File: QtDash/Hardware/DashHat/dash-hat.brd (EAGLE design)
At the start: 120.9 x 74.9 mm, 160 parts, among them IC1 LMV614, IC10 MAX9924, IC11 ZXTR2105FQ, IC2 MCP3X083008, IC3 MCP23017SS, IC4 LM358D, IC5 IL300, IC6 TSV912D, IC7 IL300, IC8 TSV912D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

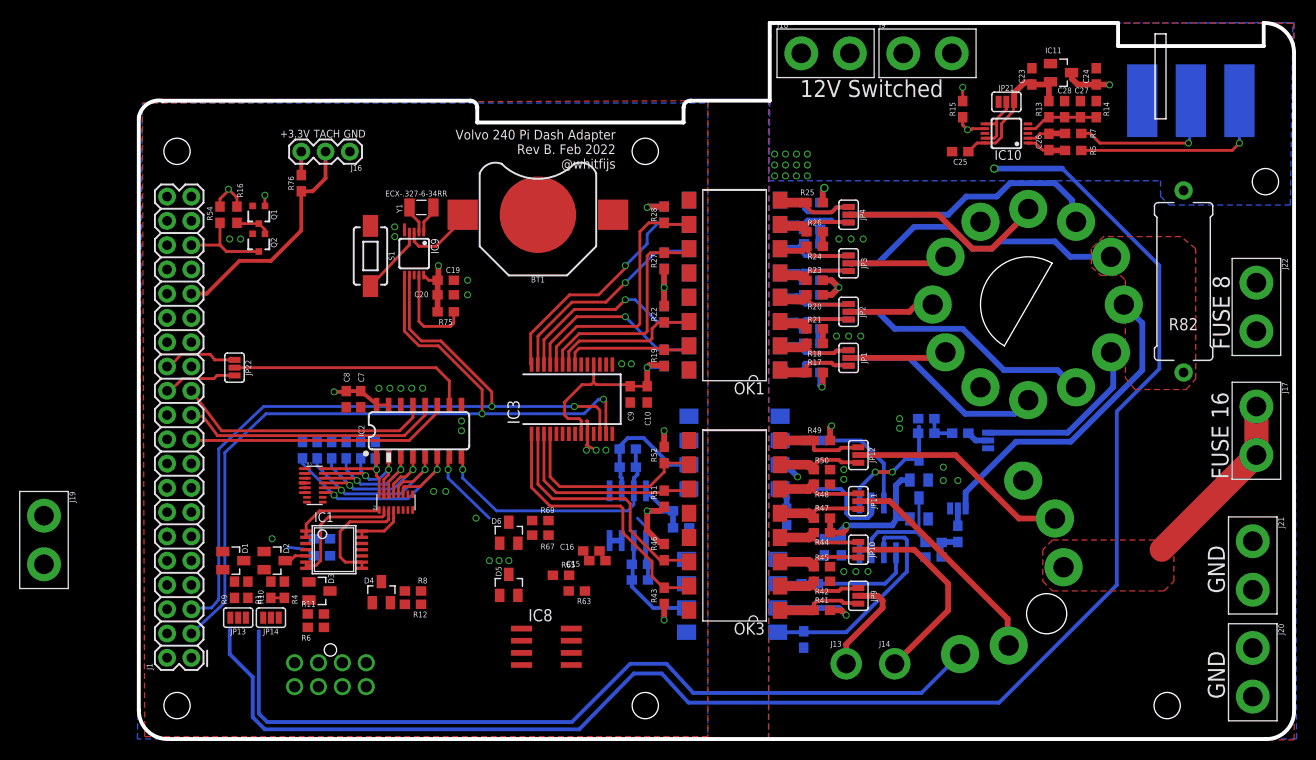
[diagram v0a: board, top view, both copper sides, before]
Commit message: topic/hardware-revc: 	- Analog input layout with new connector is done -- need to check on connector footprint as there is a dimension error 	- TODO: replace switched 12V power and GND with molex connector (right angle?)
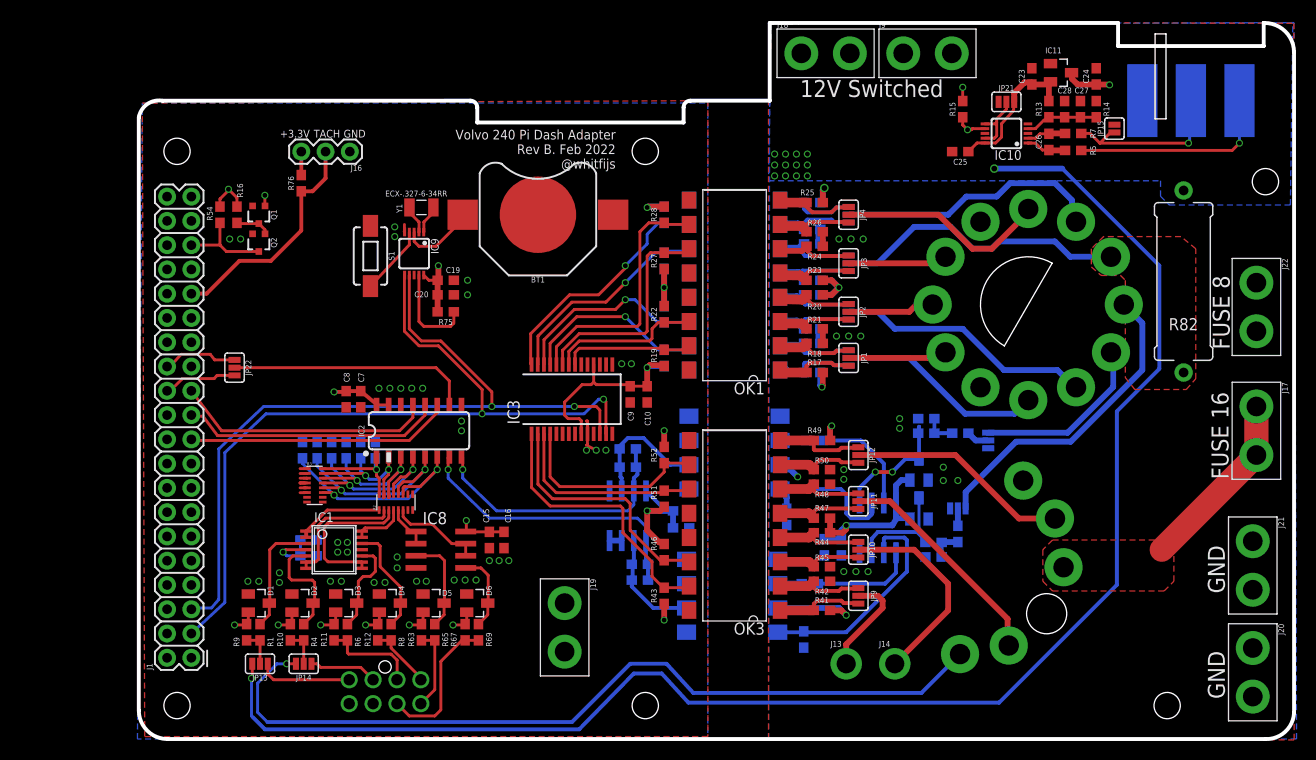
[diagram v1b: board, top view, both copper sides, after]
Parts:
- added JP15: VSS- Jumper, SparkFun-Jumpers:SMT-JUMPER_2_NO_SILK
- moved J19 55.2 mm to (44.7, 11.7)
- moved R63 16.8 mm to (29.7, 11.2), turned to 90 degrees
- moved IC8 15.0 mm to (31.8, 19.8)
- moved R65 14.5 mm to (31.1, 11.2), turned to 90 degrees
- moved R69 13.4 mm to (35.7, 11.2), turned to 90 degrees
- moved R67 12.9 mm to (34.3, 11.2), turned to 90 degrees
- moved C15 11.5 mm to (36.8, 20.8), turned to 270 degrees
- moved C16 9.22 mm to (38.4, 20.8), turned to 270 degrees
- moved D5 8.10 mm to (31.0, 14.2), turned to 270 degrees
- moved D6 8.07 mm to (35.6, 14.2), turned to 270 degrees
- moved J2 5.99 mm to (25.9, 4.95)
- moved JP14 5.92 mm to (17.4, 7.87)
- moved JP13 5.34 mm to (12.8, 7.87)
- moved D2 5.32 mm to (17.3, 14.2)
- moved D1 5.18 mm to (12.7, 14.2)
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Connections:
- net N$48 renamed VSS+
- removed net N$49: J11.1, R7.1
- new net VSS-: J11.1, JP15.1, R7.1
- net 5V: now also J2.7; no longer J2.1
- net GND-ISO: now also JP15.2
- net SENSOR4_IN: now also J2.1; no longer J2.5
- net SENSOR5_IN: now also J2.5; no longer J2.6
- net SENSOR6_IN: now also J2.6; no longer J2.7
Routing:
- net 5V: track 3.27 -> 27.2 mm, vias 0 -> 8
- net VSS-: track 0.00 -> 18.2 mm, vias 0 -> 1
- net N$49: track 16.3 -> 0.00 mm, vias 1 -> 0
- net SIG_3V3_IN1: track 15.4 -> 30.9 mm
- net SENSOR6_IN: track 0.00 -> 15.3 mm
- net N$3: track 0.00 -> 12.3 mm
- net N$15: track 0.00 -> 11.5 mm
- net SENSOR3_IN: track 0.00 -> 10.3 mm
- net N$29: track 0.00 -> 10.3 mm
- net N$11: track 0.00 -> 10.1 mm
- net SENSOR1_IN: track 0.00 -> 9.84 mm
- net N$35: track 0.00 -> 9.69 mm
- net N$7: track 2.42 -> 11.5 mm
- net SENSOR5_IN: track 0.00 -> 8.62 mm
- net N$36: track 0.17 -> 8.21 mm
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
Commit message: topic/hardware-revc: 	- added right angle nano-fit molex connector for switched 12V power 	- added 4 user inputs on the remaining 4 pins of MCP23017 	- added pwm output on pin 18 with 3.3V pullup 	- added user inputs to dash_lights.h -- likely need to pull this out and/or rework
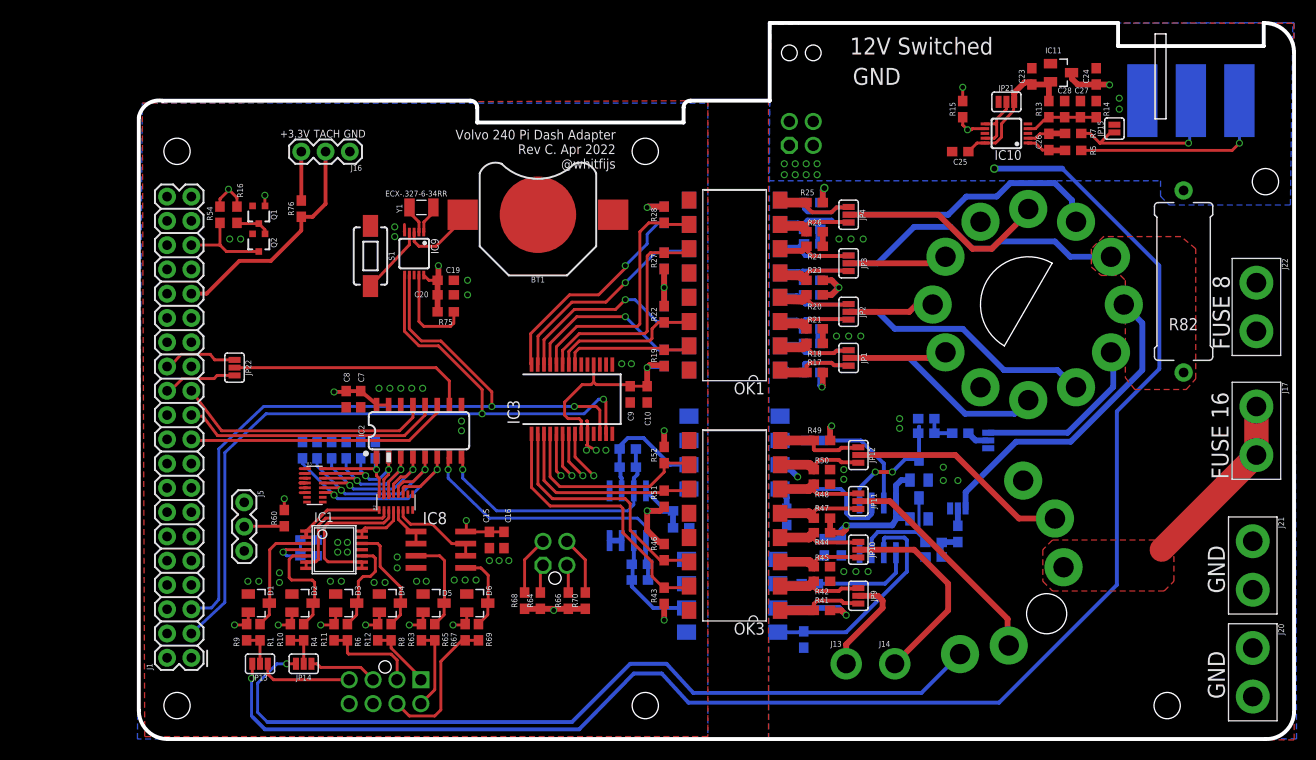
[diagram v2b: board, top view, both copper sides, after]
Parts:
- removed J18, J19, J9: (no value), SparkFun-Connectors:1X02_XTRA_BIG
- added J3: CONN_04RIGHT-ANGLE, digital_dash:MOLEX-1053141204
- added J4: CONN_04, digital_dash:MOLEX-1053101104
- added J5: PWM_OUT, SparkFun-Connectors:1X03
- added R60: 20k, digital_dash:0603
- added R64, R66, R68, R70: 1k, digital_dash:0603
- moved R76 2.67 mm to (17.1, 55.5)
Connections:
- new net GPIO18: J1.12, J5.2, R60.1
- new net USER_IN1: IC3.5, J4.1, R64.2
- new net USER_IN2: IC3.6, J4.2, R66.2
- new net USER_IN3: IC3.7, J4.3, R68.2
- new net USER_IN4: IC3.8, J4.4, R70.2
- net 12V: now also J3.1, J3.2; no longer J18.1, J18.2, J9.1, J9.2
- net 3.3V: now also R60.2, R64.1, R66.1, R68.1, R70.1
- net 5V: now also J5.3; no longer J19.2
- net GND: now also J5.1; no longer J19.1
- net GND-ISO: now also J3.3, J3.4
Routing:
- net USER_IN2: track 0.00 -> 21.6 mm, vias 0 -> 1
- net USER_IN3: track 0.00 -> 19.7 mm, vias 0 -> 1
- net USER_IN1: track 0.00 -> 19.6 mm, vias 0 -> 1
- net USER_IN4: track 0.00 -> 19.5 mm, vias 0 -> 1
- net GPIO18: track 0.00 -> 12.9 mm
- net 3.3V: track 70.9 -> 81.3 mm, vias 9 -> 11
- net AC_RELAY/VSS_TO_ECU: track 111.5 -> 113.5 mm
- net GND-ISO: vias 16 -> 18
- net 12V: vias 21 -> 17
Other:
- board text added: "Volvo 240 Pi Dash Adapter Rev C. Apr 2022 @whitfijs"
- board text removed: "Volvo 240 Pi Dash Adapter Rev B. Feb 2022 @whitfijs"

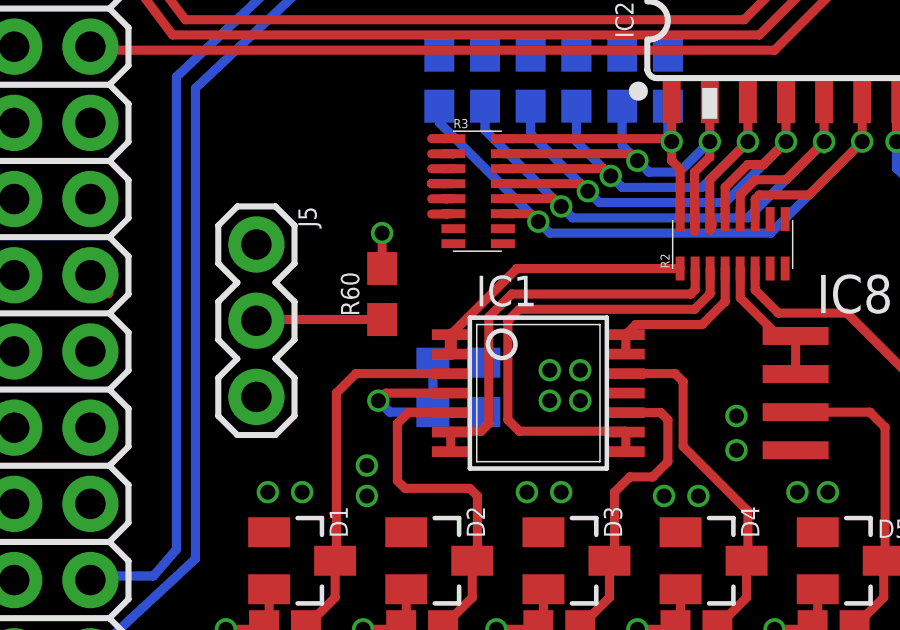
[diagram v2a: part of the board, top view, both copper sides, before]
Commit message: topic/hardware-revc: 	- small layout changes to the main board
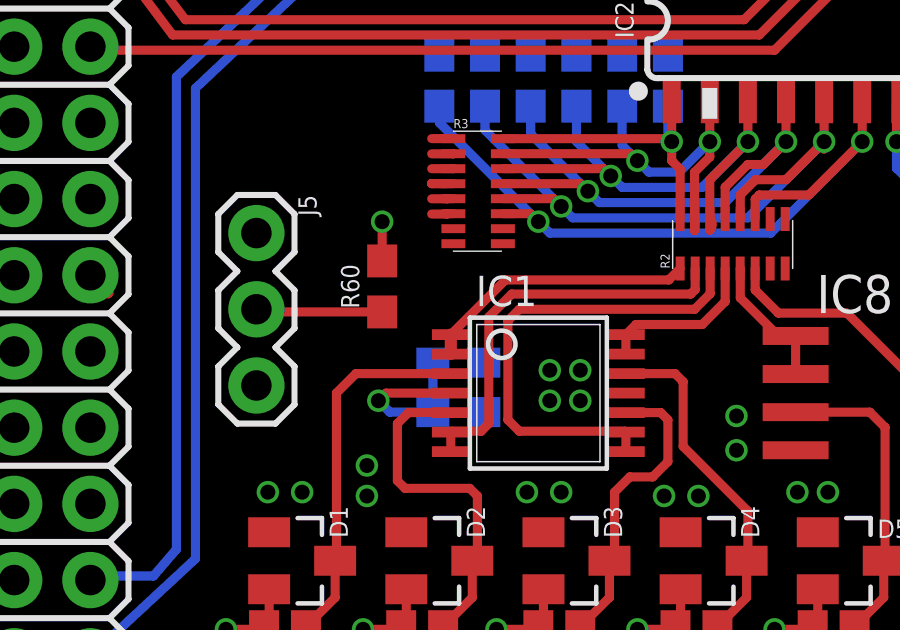
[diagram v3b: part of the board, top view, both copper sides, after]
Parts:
- moved J5 0.38 mm to (11.2, 25.1)
- moved R60 0.25 mm to (15.4, 23.4)
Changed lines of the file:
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@@
 <element name="J3" library="digital_dash" package="MOLEX-1053141204" value="CONN_04RIGHT-ANGLE" x="69.469" y="63.373"/>
 <element name="J4" library="digital_dash" package="MOLEX-1053101104" value="CONN_04" x="43.688" y="19.431" rot="R180"/>
-<element name="J5" library="SparkFun-Connectors" package="1X03" value="PWM_OUT" x="11.176" y="24.765" rot="R270">
-<attribute name="PROD_ID" value="XXX-00000" x="11.176" y="24.765" size="1.778" layer="27" rot="R270" display="off"/>
+<element name="J5" library="SparkFun-Connectors" package="1X03" value="PWM_OUT" x="11.176" y="25.146" rot="R270">
+<attribute name="PROD_ID" value="XXX-00000" x="11.176" y="25.146" size="1.778" layer="27" rot="R270" display="off"/>
 </element>
-<element name="R60" library="digital_dash" package="0603" value="20k" x="15.367" y="23.114" rot="R90"/>
+<element name="R60" library="digital_dash" package="0603" value="20k" x="15.367" y="23.368" rot="R90"/>
 <element name="R64" library="digital_dash" package="0603" value="1k" x="42.164" y="14.478" rot="R90"/>
 <element name="R66" library="digital_dash" package="0603" value="1k" x="45.085" y="14.478" rot="R90"/>
@@
 <contactref element="R2" pad="1"/>
 <wire x1="17.6562" y1="21.762" x2="17.6562" y2="21.112" width="0.4064" layer="1"/>
-<wire x1="17.6562" y1="21.762" x2="19.8592" y2="23.965" width="0.3048" layer="1"/>
-<wire x1="19.8592" y1="23.965" x2="25.301" y2="23.965" width="0.3048" layer="1"/>
+<wire x1="17.6562" y1="21.762" x2="19.4782" y2="23.584" width="0.3048" layer="1"/>
+<wire x1="19.4782" y1="23.584" x2="24.92" y2="23.584" width="0.3048" layer="1"/>
+<wire x1="24.92" y1="23.584" x2="25.301" y2="23.965" width="0.3048" layer="1"/>
 </signal>
 <signal name="ADC1_IN">
@@
 <wire x1="17.145" y1="61.468" x2="17.145" y2="56.349" width="0.4064" layer="1"/>
 <contactref element="R60" pad="2"/>
-<wire x1="15.367" y1="23.964" x2="15.367" y2="25.146" width="0.3048" layer="1"/>
-<via x="15.367" y="25.146" extent="1-16" drill="0.5"/>
+<wire x1="15.367" y1="24.218" x2="15.367" y2="25.527" width="0.3048" layer="1"/>
+<via x="15.367" y="25.527" extent="1-16" drill="0.5"/>
 <contactref element="R64" pad="1"/>
 <contactref element="R70" pad="1"/>
@@
 <contactref element="R60" pad="1"/>
 <wire x1="3.102" y1="21.2" x2="4.381" y2="22.479" width="0.3048" layer="15"/>
-<wire x1="4.381" y1="22.479" x2="9.652" y2="22.479" width="0.3048" layer="15"/>
-<wire x1="9.652" y1="22.479" x2="9.906" y2="22.225" width="0.3048" layer="15"/>
-<wire x1="9.906" y1="22.225" x2="11.176" y2="22.225" width="0.3048" layer="15"/>
-<wire x1="11.176" y1="22.225" x2="11.469" y2="22.264" width="0.3048" layer="1"/>
-<wire x1="11.469" y1="22.264" x2="15.367" y2="22.264" width="0.3048" layer="1"/>
+<wire x1="4.381" y1="22.479" x2="9.906" y2="22.479" width="0.3048" layer="15"/>
+<wire x1="9.906" y1="22.479" x2="11.176" y2="22.606" width="0.3048" layer="15"/>
+<wire x1="11.176" y1="22.606" x2="11.723" y2="22.518" width="0.3048" layer="1"/>
+<wire x1="11.723" y1="22.518" x2="15.367" y2="22.518" width="0.3048" layer="1"/>
 </signal>
 </signals>
